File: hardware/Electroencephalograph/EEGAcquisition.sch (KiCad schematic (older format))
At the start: 44 parts, among them U1 ADS1298IPAG, U2 OPA330xxD, U4 REF5025, U5 OPA350, X1 2M048

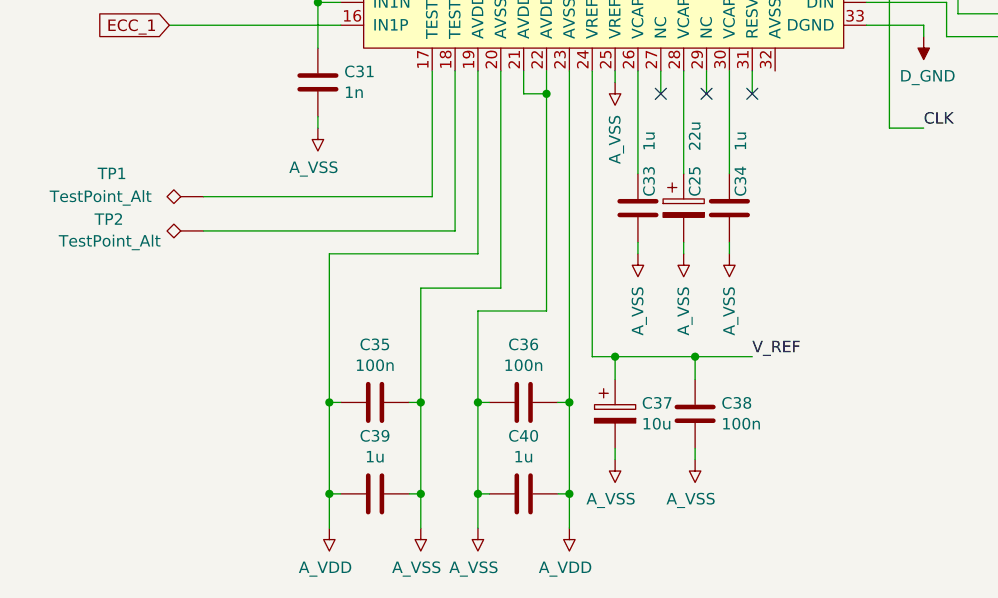
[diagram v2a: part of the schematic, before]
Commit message: power circuit supply added
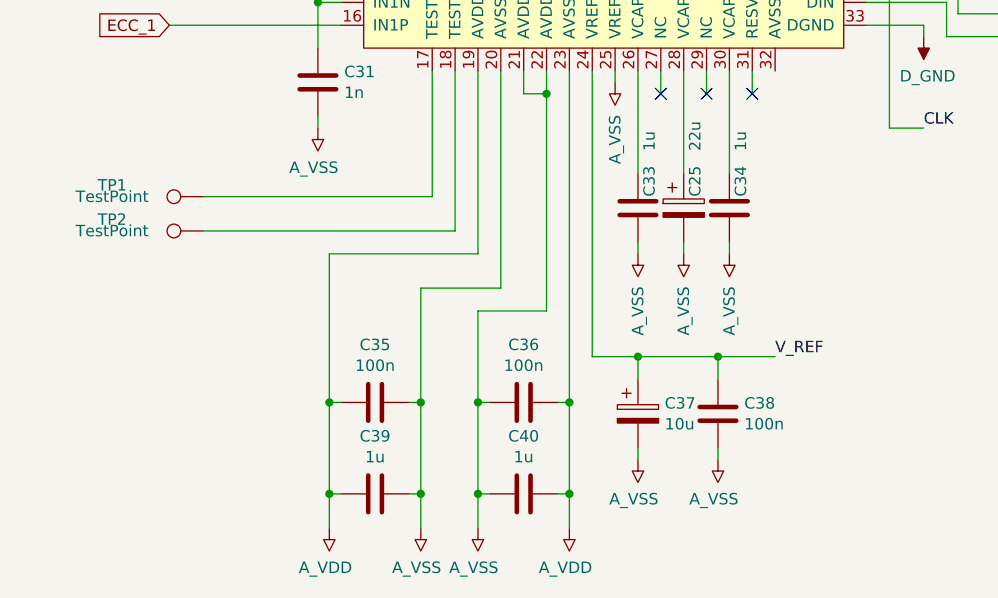
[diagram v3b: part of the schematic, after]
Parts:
- removed TP1, TP2: TestPoint_Alt, TestPoint:TestPoint_Pad_2.5x2.5mm, symbol Connector:TestPoint_Alt
- added TP1, TP2: TestPoint, TestPoint:TestPoint_Pad_1.5x1.5mm, symbol Connector:TestPoint
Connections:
- net at U1.17 (TESTP_PACE_OUT1): now also TP1.1
- net at U1.18 (TESTN_PACE_OUT2): now also TP2.1
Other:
- moved on the sheet: C37, C38
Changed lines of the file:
@@
 $Descr A4 11693 8268
 encoding utf-8
-Sheet 3 5
+Sheet 3 6
 Title ""
 Date ""
@@
 	4250 2250 4450 2250
 $Comp
-L Device:LED D20
-U 1 1 5E0FF9B1
-P 5700 4100
-F 0 "D20" H 5550 4200 50  0000 C CNN
-F 1 "LED" H 5750 4200 50  0000 C CNN
-F 2 "LED_SMD:LED_0603_1608Metric" H 5700 4100 50  0001 C CNN
-F 3 "~" H 5700 4100 50  0001 C CNN
-	1    5700 4100
-	-1   0    0    1
-$EndComp
-$Comp
 L Device:LED D19
 U 1 1 5E100F32
@@
 $EndComp
 $Comp
-L Device:R R?
-U 1 1 5E10C2CB
-P 5300 4100
-AR Path="/5E10C2CB" Ref="R?"  Part="1"
-AR Path="/5DF4CFF8/5E10C2CB" Ref="R?"  Part="1"
-AR Path="/5DF61103/5E10C2CB" Ref="R36"  Part="1"
-F 0 "R36" V 5093 4100 50  0000 C CNN
-F 1 "220R" V 5184 4100 50  0000 C CNN
-F 2 "Resistor_SMD:R_0402_1005Metric" V 5230 4100 50  0001 C CNN
-F 3 "~" H 5300 4100 50  0001 C CNN
-	1    5300 4100
-	0    1    1    0
-$EndComp
-$Comp
 L Electroencephalograph:D_GND #PWR67
 U 1 1 5E10C764
@@
 	1    0    0    -1
 $EndComp
-$Comp
-L Electroencephalograph:D_GND #PWR69
-U 1 1 5E10CCA3
-P 6150 4150
-F 0 "#PWR69" H 6150 4175 50  0001 C CNN
-F 1 "D_GND" H 6167 3977 50  0000 C CNN
-F 2 "" H 6150 4175 50  0001 C CNN
-F 3 "" H 6150 4175 50  0001 C CNN
-	1    6150 4150
-	1    0    0    -1
-$EndComp
 Wire Wire Line
 	5450 3200 5550 3200
@@
 	6150 3800 6150 3850
 Wire Wire Line
-	5450 4100 5550 4100
-Wire Wire Line
-	5850 4100 6150 4100
-Wire Wire Line
-	6150 4100 6150 4150
-Wire Wire Line
 	4150 3800 4800 3800
 Wire Wire Line
@@
 Wire Wire Line
 	5100 4200 5100 4100
-Wire Wire Line
-	5100 4100 5150 4100
 Text GLabel 4900 4650 2    50   Output ~ 0
 SPI_CLK
@@
 L Device:C C?
 U 1 1 5E1499A4
-P 3400 6800
+P 3500 6800
 AR Path="/5DF4CFF8/5E1499A4" Ref="C?"  Part="1"
 AR Path="/5DF61103/5E1499A4" Ref="C38"  Part="1"
-F 0 "C38" H 3515 6846 50  0000 L CNN
-F 1 "100n" H 3515 6755 50  0000 L CNN
-F 2 "Capacitor_SMD:C_0402_1005Metric" H 3438 6650 50  0001 C CNN
-F 3 "~" H 3400 6800 50  0001 C CNN
-	1    3400 6800
+F 0 "C38" H 3615 6846 50  0000 L CNN
+F 1 "100n" H 3615 6755 50  0000 L CNN
+F 2 "Capacitor_SMD:C_0402_1005Metric" H 3538 6650 50  0001 C CNN
+F 3 "~" H 3500 6800 50  0001 C CNN
+	1    3500 6800
 	1    0    0    -1
 $EndComp
@@
 L Device:CP C?
 U 1 1 5E149E75
-P 3050 6800
+P 3150 6800
 AR Path="/5DF4CFF8/5E149E75" Ref="C?"  Part="1"
 AR Path="/5DF61103/5E149E75" Ref="C37"  Part="1"
-F 0 "C37" H 3167 6846 50  0000 L CNN
-F 1 "10u" H 3167 6755 50  0000 L CNN
-F 2 "Capacitor_Tantalum_SMD:CP_EIA-3528-21_Kemet-B" H 3088 6650 50  0001 C CNN
-F 3 "~" H 3050 6800 50  0001 C CNN
-	1    3050 6800
+F 0 "C37" H 3267 6846 50  0000 L CNN
+F 1 "10u" H 3267 6755 50  0000 L CNN
+F 2 "Capacitor_Tantalum_SMD:CP_EIA-3528-21_Kemet-B" H 3188 6650 50  0001 C CNN
+F 3 "~" H 3150 6800 50  0001 C CNN
+	1    3150 6800
 	1    0    0    -1
 $EndComp
@@
 	3050 5300 3050 5350
 Wire Wire Line
-	3400 6550 3400 6650
+	3500 6550 3500 6650
 Wire Wire Line
 	3350 5300 3350 5750
@@
 	3150 5300 3150 5750
 Wire Wire Line
-	3050 6550 3050 6650
+	3150 6550 3150 6650
 Wire Wire Line
 	3250 5300 3250 5400
@@
 L Electroencephalograph:A_VSS #PWR70
 U 1 1 5E1AAFE9
-P 3400 7000
-F 0 "#PWR70" H 3400 7000 50  0001 C CNN
-F 1 "A_VSS" H 3418 7173 50  0000 C CNN
-F 2 "" H 3400 7000 50  0001 C CNN
-F 3 "" H 3400 7000 50  0001 C CNN
-	1    3400 7000
+P 3500 7000
+F 0 "#PWR70" H 3500 7000 50  0001 C CNN
+F 1 "A_VSS" H 3518 7173 50  0000 C CNN
+F 2 "" H 3500 7000 50  0001 C CNN
+F 3 "" H 3500 7000 50  0001 C CNN
+	1    3500 7000
 	-1   0    0    1
 $EndComp
@@
 L Electroencephalograph:A_VSS #PWR65
 U 1 1 5E1AB505
-P 3050 7000
-F 0 "#PWR65" H 3050 7000 50  0001 C CNN
-F 1 "A_VSS" H 3068 7173 50  0000 C CNN
-F 2 "" H 3050 7000 50  0001 C CNN
-F 3 "" H 3050 7000 50  0001 C CNN
-	1    3050 7000
-	-1   0    0    1
-$EndComp
-Wire Wire Line
-	3400 7000 3400 6950
-Wire Wire Line
-	3050 7000 3050 6950
+P 3150 7000
+F 0 "#PWR65" H 3150 7000 50  0001 C CNN
+F 1 "A_VSS" H 3168 7173 50  0000 C CNN
+F 2 "" H 3150 7000 50  0001 C CNN
+F 3 "" H 3150 7000 50  0001 C CNN
+	1    3150 7000
+	-1   0    0    1
+$EndComp
+Wire Wire Line
+	3500 7000 3500 6950
+Wire Wire Line
+	3150 7000 3150 6950
 Wire Wire Line
 	3650 5300 3650 5400
@@
 Wire Wire Line
 	5400 4300 5400 4350
-$Comp
-L Connector:TestPoint_Alt TP1
-U 1 1 5E2F9E37
-P 1250 5850
-F 0 "TP1" V 1350 6250 50  0000 C CNN
-F 1 "TestPoint_Alt" V 1250 6300 50  0000 C CNN
-F 2 "TestPoint:TestPoint_Pad_2.5x2.5mm" H 1450 5850 50  0001 C CNN
-F 3 "~" H 1450 5850 50  0001 C CNN
-	1    1250 5850
-	0    -1   -1   0
-$EndComp
-$Comp
-L Connector:TestPoint_Alt TP2
-U 1 1 5E2FAD46
-P 1250 6000
-F 0 "TP2" V 1300 6350 50  0000 L CNN
-F 1 "TestPoint_Alt" V 1205 6187 50  0000 L CNN
-F 2 "TestPoint:TestPoint_Pad_2.5x2.5mm" H 1450 6000 50  0001 C CNN
-F 3 "~" H 1450 6000 50  0001 C CNN
-	1    1250 6000
-	0    -1   -1   0
-$EndComp
 Wire Wire Line
 	2250 5300 2250 5850
@@
 	10650 1450 10850 1450
 Wire Wire Line
-	2950 6550 3050 6550
-Connection ~ 3050 6550
-Wire Wire Line
-	3050 6550 3400 6550
-Wire Wire Line
-	3400 6550 3650 6550
-Connection ~ 3400 6550
+	2950 6550 3150 6550
+Connection ~ 3150 6550
+Wire Wire Line
+	3150 6550 3500 6550
+Wire Wire Line
+	3500 6550 3750 6550
+Connection ~ 3500 6550
 Wire Wire Line
 	4150 4800 4600 4800
@@
 Text Label 4400 5550 0    50   ~ 0
 CLK
-Text Label 3650 6550 0    50   ~ 0
+Text Label 3750 6550 0    50   ~ 0
 V_REF
 Wire Wire Line
 	2850 5300 2850 6750
+$Comp
+L Connector:TestPoint TP1
+U 1 1 5E170075
+P 1250 5850
+F 0 "TP1" V 1300 6250 50  0000 C CNN
+F 1 "TestPoint" V 1250 6250 50  0000 C CNN
+F 2 "TestPoint:TestPoint_Pad_1.5x1.5mm" H 1450 5850 50  0001 C CNN
+F 3 "~" H 1450 5850 50  0001 C CNN
+	1    1250 5850
+	0    -1   -1   0
+$EndComp
+$Comp
+L Connector:TestPoint TP2
+U 1 1 5E19AC83
+P 1250 6000
+F 0 "TP2" V 1300 6400 50  0000 C CNN
+F 1 "TestPoint" V 1250 6400 50  0000 C CNN
+F 2 "TestPoint:TestPoint_Pad_1.5x1.5mm" H 1450 6000 50  0001 C CNN
+F 3 "~" H 1450 6000 50  0001 C CNN
+	1    1250 6000
+	0    -1   -1   0
+$EndComp
+Wire Wire Line
+	5100 4100 5150 4100
+Wire Wire Line
+	6150 4100 6150 4150
+Wire Wire Line
+	5850 4100 6150 4100
+Wire Wire Line
+	5450 4100 5550 4100
+$Comp
+L Electroencephalograph:D_GND #PWR69
+U 1 1 5E10CCA3
+P 6150 4150
+F 0 "#PWR69" H 6150 4175 50  0001 C CNN
+F 1 "D_GND" H 6167 3977 50  0000 C CNN
+F 2 "" H 6150 4175 50  0001 C CNN
+F 3 "" H 6150 4175 50  0001 C CNN
+	1    6150 4150
+	1    0    0    -1
+$EndComp
+$Comp
+L Device:R R?
+U 1 1 5E10C2CB
+P 5300 4100
+AR Path="/5E10C2CB" Ref="R?"  Part="1"
+AR Path="/5DF4CFF8/5E10C2CB" Ref="R?"  Part="1"
+AR Path="/5DF61103/5E10C2CB" Ref="R36"  Part="1"
+F 0 "R36" V 5093 4100 50  0000 C CNN
+F 1 "220R" V 5184 4100 50  0000 C CNN
+F 2 "Resistor_SMD:R_0402_1005Metric" V 5230 4100 50  0001 C CNN
+F 3 "~" H 5300 4100 50  0001 C CNN
+	1    5300 4100
+	0    1    1    0
+$EndComp
+$Comp
+L Device:LED D20
+U 1 1 5E0FF9B1
+P 5700 4100
+F 0 "D20" H 5550 4200 50  0000 C CNN
+F 1 "LED" H 5750 4200 50  0000 C CNN
+F 2 "LED_SMD:LED_0603_1608Metric" H 5700 4100 50  0001 C CNN
+F 3 "~" H 5700 4100 50  0001 C CNN
+	1    5700 4100
+	-1   0    0    1
+$EndComp
 $EndSCHEMATC

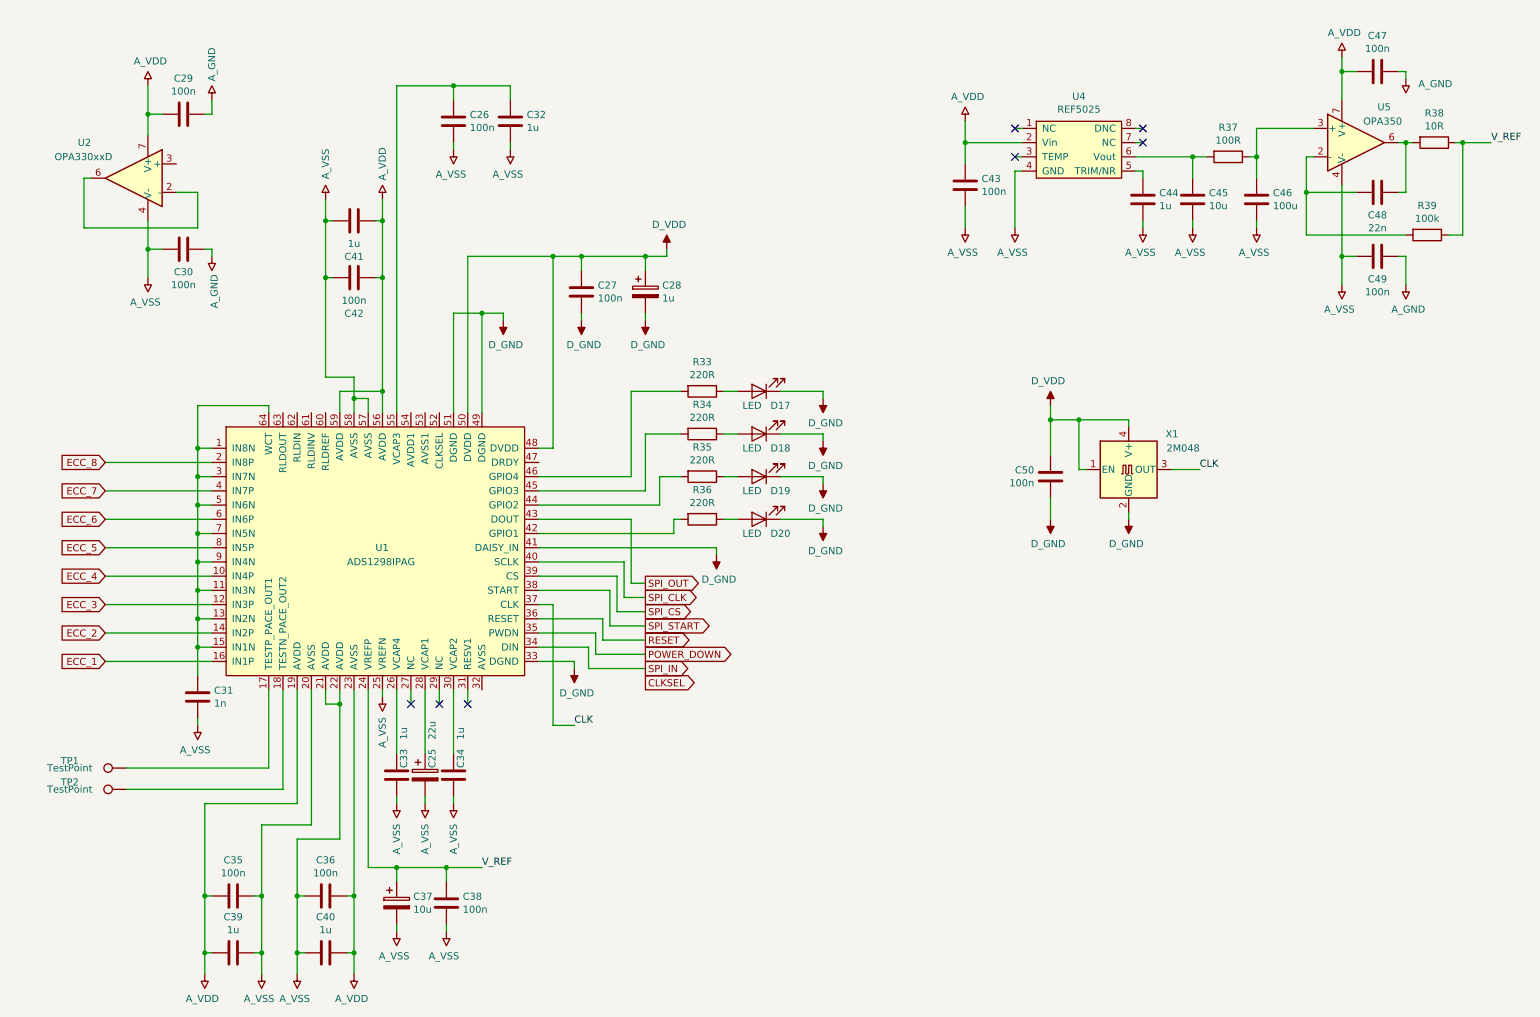
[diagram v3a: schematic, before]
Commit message: enqable separate electrodes for each point
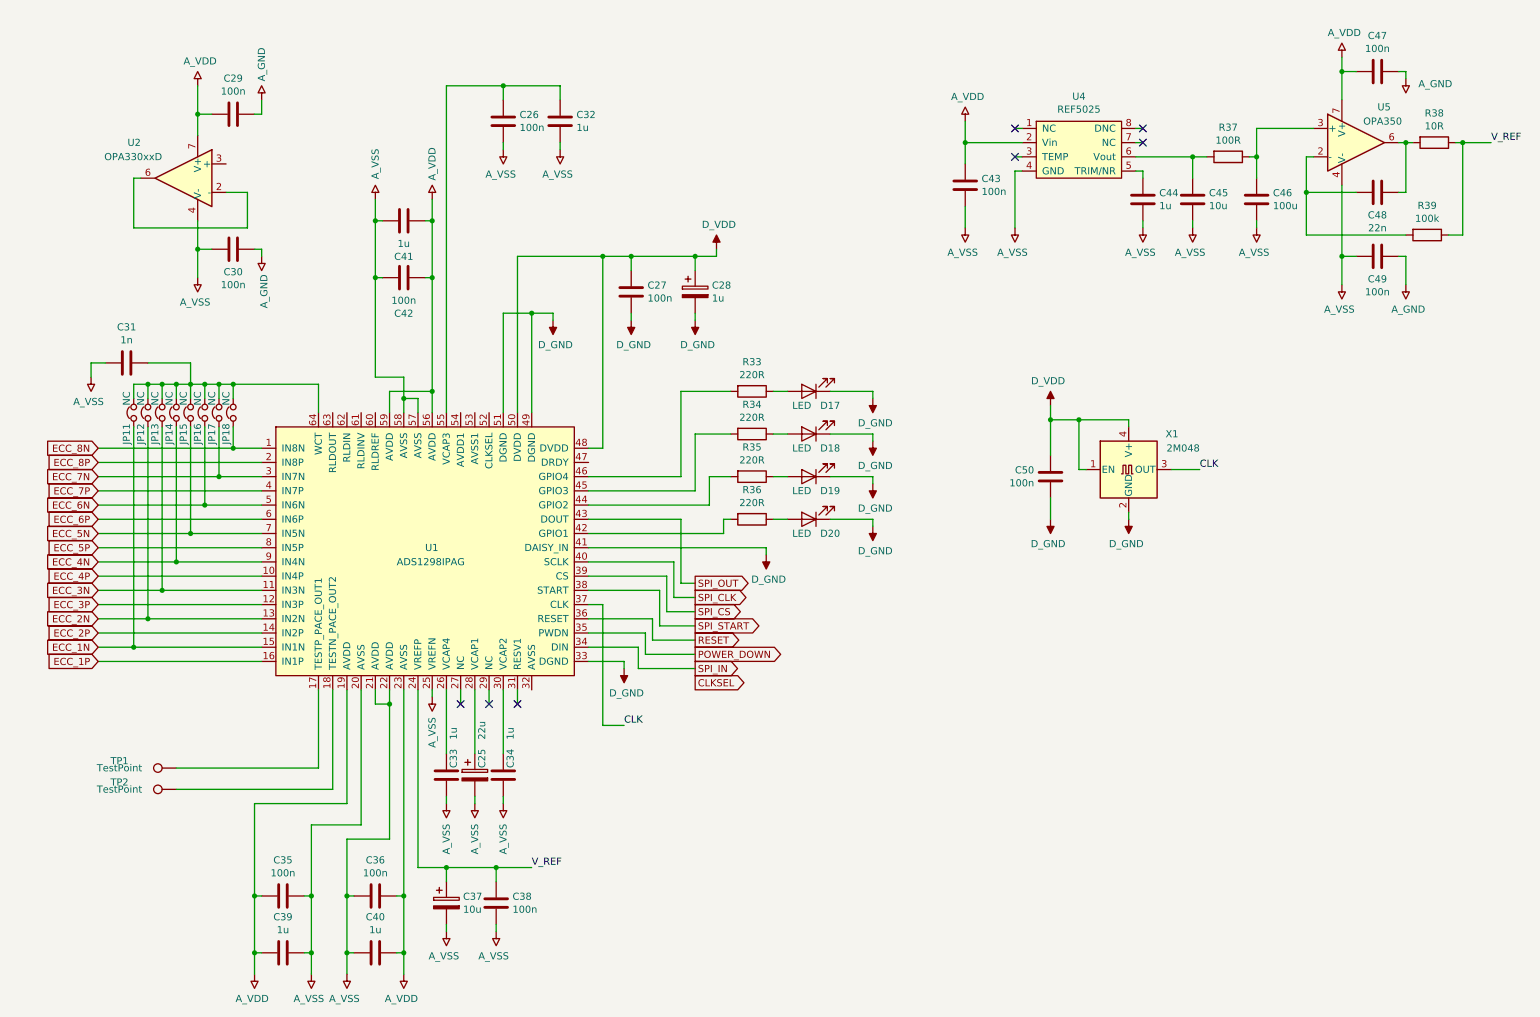
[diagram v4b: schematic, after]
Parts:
- added JP11, JP12, JP13, JP14, JP15, JP16, JP17, JP18: NC, Jumper:SolderJumper-2_P1.3mm_Bridged_Pad1.0x1.5mm, symbol Device:Jumper_NC_Small
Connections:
- net ECC_1 renamed ECC_1P
- net ECC_2 renamed ECC_2P
- net ECC_3 renamed ECC_3P
- net ECC_4 renamed ECC_4P
- net ECC_5 renamed ECC_5P
- net ECC_6 renamed ECC_6P
- net ECC_7 renamed ECC_7P
- net ECC_8 renamed ECC_8P
- new net: C31.1, JP11.1, JP12.1, JP13.1, JP14.1, JP15.1, JP16.1, JP17.1, JP18.1, U1.64 (WCT)
- new net ECC_1N: JP11.2, U1.15 (IN1N)
- new net ECC_2N: JP12.2, U1.13 (IN2N)
- new net ECC_3N: JP13.2, U1.11 (IN3N)
- new net ECC_4N: JP14.2, U1.9 (IN4N)
- new net ECC_5N: JP15.2, U1.7 (IN5N)
- new net ECC_6N: JP16.2, U1.5 (IN6N)
- new net ECC_7N: JP17.2, U1.3 (IN7N)
- new net ECC_8N: JP18.2, U1.1 (IN8N)
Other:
- moved on the sheet: C25, C26, C27, C28, C29, C30, C31, C32, C33, C34, C35, C36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
